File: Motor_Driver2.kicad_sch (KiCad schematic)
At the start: 20 parts, among them J701 Conn_01x02_Socket, U701 DMHT6016LFJ-13, U702 DRV8701

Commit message: all layouts re-designed.Next step routing...
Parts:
- C704: footprint Capacitor_SMD:C_Elec_8x10.2 -> Capacitor_SMD:CP_Elec_8x10; now left out of the parts list
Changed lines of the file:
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@@
 		(at 156.5298 86.0634 0)
 		(unit 1)
-		(exclude_from_sim no)
-		(in_bom yes)
-		(on_board yes)
+		(exclude_from_sim yes)
+		(in_bom no)
+		(on_board no)
 		(dnp no)
 		(property "Reference" "C704"
@@
 			)
 		)
-		(property "Footprint" "Capacitor_SMD:C_Elec_8x10.2"
+		(property "Footprint" "Capacitor_SMD:CP_Elec_8x10"
 			(at 156.5298 86.0634 0)
 			(effects

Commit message: ethernet, usb and motor driver-2 block routed, analog and digital planes seperated
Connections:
- net GND: now also U702.25 (GND)
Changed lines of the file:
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@@
 	(wire
 		(pts
+			(xy 132.4884 129.4869) (xy 135.7764 129.4869)
+		)
+		(stroke
+			(width 0)
+			(type default)
+		)
+	)
+	(wire
+		(pts
 			(xy 88.1048 90.2456) (xy 97.0671 90.2456)
 		)
@@
 	(wire
 		(pts
+			(xy 135.7764 129.4869) (xy 135.7764 139.1714)
+		)
+		(stroke
+			(width 0)
+			(type default)
+		)
+	)
+	(wire
+		(pts
 			(xy 119.8075 79.9351) (xy 119.8075 78.631)
 		)
@@
 	(wire
 		(pts
+			(xy 135.843 139.1714) (xy 135.7764 139.1714)
+		)
+		(stroke
+			(width 0)
+			(type default)
+		)
+	)
+	(wire
+		(pts
 			(xy 225.0723 120.7755) (xy 225.0723 121.7812)
 		)
@@
 		(pin "5"
 		)
+		(pin "25"
+		)
 		(instances
 			(project "mixed signal board project"
@@
 					(unit 1)
 				)
+			)
+		)
+	)
+	(symbol
+		(lib_id "power:GND")
+		(at 135.843 139.1714 0)
+		(unit 1)
+		(exclude_from_sim no)
+		(in_bom yes)
+		(on_board yes)
+		(dnp no)
+		(property "Reference" "#PWR0416"
+			(at 135.843 145.5214 0)
+			(effects
+				(font
+					(size 1.27 1.27)
+				)
+				(hide yes)
+			)
+		)
+		(property "Value" "GND"
+			(at 135.99 142.8958 0)
+			(effects
+				(font
+					(size 1.27 1.27)
+				)
+			)
+		)
+		(property "Footprint" ""
+			(at 135.843 139.1714 0)
+			(effects
+				(font
+					(size 1.27 1.27)
+				)
+				(hide yes)
+			)
+		)
+		(property "Datasheet" ""
+			(at 135.843 139.1714 0)
+			(effects
+				(font
+					(size 1.27 1.27)
+				)
+				(hide yes)
+			)
+		)
+		(property "Description" "Power symbol creates a global label with name \"GND\" , ground"
+			(at 135.843 139.1714 0)
+			(effects
+				(font
+					(size 1.27 1.27)
+				)
+				(hide yes)
+			)
+		)
+		(pin "1"
+		)
+		(instances
+			(project "mixed signal board project"
+				(path "/8a424437-6f3e-424c-a786-3b8b285eee60/fd70bbc0-4293-4cb1-946c-bcfbb1973be8"
+					(reference "#PWR0416")
+					(unit 1)
+				)

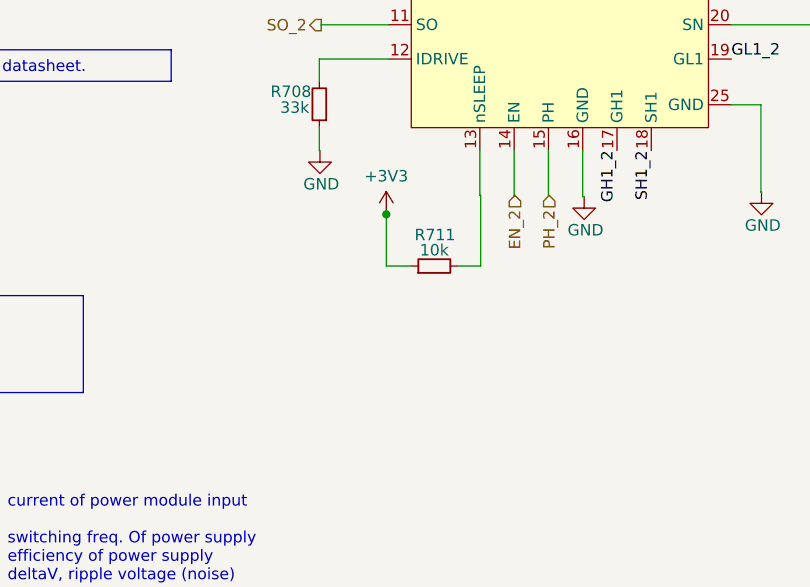
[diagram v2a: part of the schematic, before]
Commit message: motor driver nsleep pin pull-up resistor connected 12V plane by 3.3V voltage divider.
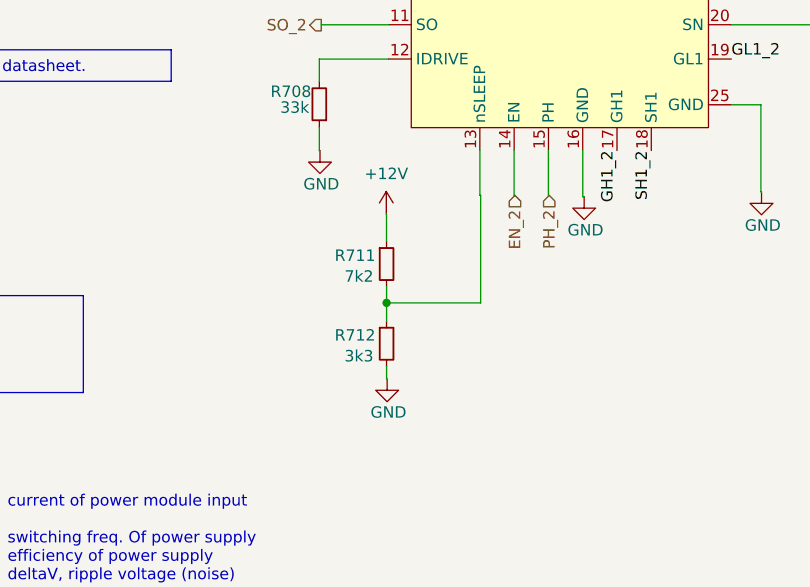
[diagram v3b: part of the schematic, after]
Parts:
- added R712: 3k3, Resistor_SMD:R_0805_2012Metric_Pad1.20x1.40mm_HandSolder, symbol Device:R_Small
- R711: value 10k -> 7k2
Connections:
- net +3V3 is gone; now on net +12V: R711.1
- net GND: now also R712.2
- net at R711.2, U702.13 (nSLEEP): now also R712.1
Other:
- moved on the sheet: R711
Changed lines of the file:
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@@
-	)
-	(junction
-		(at 94.1551 141.6614)
-		(diameter 0)
-		(color 0 0 0 0)
 	)
 	(junction
@@
 	)
 	(junction
+		(at 94.1837 151.4988)
+		(diameter 0)
+		(color 0 0 0 0)
+	)
+	(junction
 		(at 143.8069 81.3086)
 		(diameter 0)
@@
 	(wire
 		(pts
+			(xy 94.1757 141.6614) (xy 94.1757 144.6437)
+		)
+		(stroke
+			(width 0)
+			(type default)
+		)
+	)
+	(wire
+		(pts
 			(xy 59.9681 90.275) (xy 59.9681 92.1803)
 		)
@@
 	(wire
 		(pts
+			(xy 94.1837 158.58) (xy 94.1837 159.9414)
+		)
+		(stroke
+			(width 0)
+			(type default)
+		)
+	)
+	(wire
+		(pts
 			(xy 64.968 115.5816) (xy 64.968 116.7869)
 		)
@@
 	(wire
 		(pts
+			(xy 94.1837 159.9414) (xy 94.2463 159.9414)
+		)
+		(stroke
+			(width 0)
+			(type default)
+		)
+	)
+	(wire
+		(pts
 			(xy 168.1415 150.7108) (xy 168.0399 150.7108)
 		)
@@
 	(wire
 		(pts
-			(xy 94.1551 147.4049) (xy 94.1551 141.6614)
-		)
-		(stroke
-			(width 0)
-			(type default)
-		)
-	)
-	(wire
-		(pts
 			(xy 65.0488 109.1669) (xy 60.5986 109.1669)
 		)
@@
 	(wire
 		(pts
+			(xy 94.1757 144.6437) (xy 94.1837 144.6437)
+		)
+		(stroke
+			(width 0)
+			(type default)
+		)
+	)
+	(wire
+		(pts
+			(xy 94.1837 151.4988) (xy 94.1837 153.5)
+		)
+		(stroke
+			(width 0)
+			(type default)
+		)
+	)
+	(wire
+		(pts
 			(xy 159.0733 126.3206) (xy 163.1338 126.3206)
 		)
@@
 	(wire
 		(pts
-			(xy 102.0283 147.4049) (xy 104.6392 147.4049)
-		)
-		(stroke
-			(width 0)
-			(type default)
-		)
-	)
-	(wire
-		(pts
 			(xy 156.5298 90.2469) (xy 143.57 90.2469)
 		)
@@
 	(wire
 		(pts
+			(xy 104.6392 151.4988) (xy 94.1837 151.4988)
+		)
+		(stroke
+			(width 0)
+			(type default)
+		)
+	)
+	(wire
+		(pts
 			(xy 123.5984 91.8686) (xy 130.6565 91.8686)
 		)
@@
 	(wire
 		(pts
+			(xy 94.1837 149.7237) (xy 94.1837 151.4988)
+		)
+		(stroke
+			(width 0)
+			(type default)
+		)
+	)
+	(wire
+		(pts
 			(xy 79.5667 90.2852) (xy 70.2699 90.2852)
 		)
@@
 	(wire
 		(pts
+			(xy 104.6392 139.5566) (xy 104.6392 151.4988)
+		)
+		(stroke
+			(width 0)
+			(type default)
+		)
+	)
+	(wire
+		(pts
 			(xy 143.8069 81.3086) (xy 153.544 81.3086)
 		)
@@
 	(wire
 		(pts
-			(xy 96.9483 147.4049) (xy 94.1551 147.4049)
-		)
-		(stroke
-			(width 0)
-			(type default)
-		)
-	)
-	(wire
-		(pts
 			(xy 116.6311 78.6426) (xy 116.6837 88.2698)
 		)
@@
 		(pts
 			(xy 220.0448 116.7012) (xy 216.346 116.7012)
-		)
-		(stroke
-			(width 0)
-			(type default)
-		)
-	)
-	(wire
-		(pts
-			(xy 104.6392 147.4049) (xy 104.6392 139.5566)
 		)
 		(stroke
@@
 	(symbol
 		(lib_id "Device:R_Small")
-		(at 99.4883 147.4049 90)
+		(at 94.1837 147.1837 0)
 		(unit 1)
 		(exclude_from_sim no)
@@
 		(dnp no)
 		(property "Reference" "R711"
-			(at 99.5589 143.9472 90)
-			(effects
-				(font
-					(size 1.27 1.27)
-				)
-			)
-		)
-		(property "Value" "10k"
-			(at 99.4883 145.6408 90)
+			(at 90.6816 146.2457 0)
+			(effects
+				(font
+					(size 1.27 1.27)
+				)
+			)
+		)
+		(property "Value" "7k2"
+			(at 91.1194 148.5596 0)
 			(effects
 				(font
@@
 		)
 		(property "Footprint" "Resistor_SMD:R_0805_2012Metric_Pad1.20x1.40mm_HandSolder"
-			(at 99.4883 147.4049 0)
+			(at 94.1837 147.1837 0)
 			(effects
 				(font
@@
 		)
 		(property "Datasheet" "~"
-			(at 99.4883 147.4049 0)
+			(at 94.1837 147.1837 0)
 			(effects
 				(font
@@
 		)
 		(property "Description" "Resistor, small symbol"
-			(at 99.4883 147.4049 0)
+			(at 94.1837 147.1837 0)
 			(effects
 				(font
@@
 				(path "/8a424437-6f3e-424c-a786-3b8b285eee60/fd70bbc0-4293-4cb1-946c-bcfbb1973be8"
 					(reference "R701")
+					(unit 1)
+				)
+			)
+		)
+	)
+	(symbol
+		(lib_id "power:GND")
+		(at 94.2463 159.9414 0)
+		(unit 1)
+		(exclude_from_sim no)
+		(in_bom yes)
+		(on_board yes)
+		(dnp no)
+		(property "Reference" "#PWR0809"
+			(at 94.2463 166.2914 0)
+			(effects
+				(font
+					(size 1.27 1.27)
+				)
+				(hide yes)
+			)
+		)
+		(property "Value" "GND"
+			(at 94.3933 163.6658 0)
+			(effects
+				(font
+					(size 1.27 1.27)
+				)
+			)
+		)
+		(property "Footprint" ""
+			(at 94.2463 159.9414 0)
+			(effects
+				(font
+					(size 1.27 1.27)
+				)
+				(hide yes)
+			)
+		)
+		(property "Datasheet" ""
+			(at 94.2463 159.9414 0)
+			(effects
+				(font
+					(size 1.27 1.27)
+				)
+				(hide yes)
+			)
+		)
+		(property "Description" "Power symbol creates a global label with name \"GND\" , ground"
+			(at 94.2463 159.9414 0)
+			(effects
+				(font
+					(size 1.27 1.27)
+				)
+				(hide yes)
+			)
+		)
+		(pin "1"
+		)
+		(instances
+			(project "mixed signal board project"
+				(path "/8a424437-6f3e-424c-a786-3b8b285eee60/fd70bbc0-4293-4cb1-946c-bcfbb1973be8"
+					(reference "#PWR0809")
 					(unit 1)
 				)
@@
 	)
 	(symbol
+		(lib_id "Device:R_Small")
+		(at 94.1837 156.04 0)
+		(unit 1)
+		(exclude_from_sim no)
+		(in_bom yes)
+		(on_board yes)
+		(dnp no)
+		(property "Reference" "R712"
+			(at 90.6816 155.102 0)
+			(effects
+				(font
+					(size 1.27 1.27)
+				)
+			)
+		)
+		(property "Value" "3k3"
+			(at 91.1194 157.4159 0)
+			(effects
+				(font
+					(size 1.27 1.27)
+				)
+			)
+		)
+		(property "Footprint" "Resistor_SMD:R_0805_2012Metric_Pad1.20x1.40mm_HandSolder"
+			(at 94.1837 156.04 0)
+			(effects
+				(font
+					(size 1.27 1.27)
+				)
+				(hide yes)
+			)
+		)
+		(property "Datasheet" "~"
+			(at 94.1837 156.04 0)
+			(effects
+				(font
+					(size 1.27 1.27)
+				)
+				(hide yes)
+			)
+		)
+		(property "Description" "Resistor, small symbol"
+			(at 94.1837 156.04 0)
+			(effects
+				(font
+					(size 1.27 1.27)
+				)
+				(hide yes)
+			)
+		)
+		(pin "1"
+		)
+		(pin "2"
+		)
+		(instances
+			(project "mixed signal board project"
+				(path "/8a424437-6f3e-424c-a786-3b8b285eee60/fd70bbc0-4293-4cb1-946c-bcfbb1973be8"
+					(reference "R712")
+					(unit 1)
+				)
+			)
+		)
+	)
+	(symbol
 		(lib_id "power:GND")
 		(at 168.0399 150.7108 0)
@@
 			)
 		)
-		(property "Value" "+3V3"
-			(at 94.1551 137.42 0)
-			(effects
-				(font
+		(property "Value" "+12V"
+			(at 94.1551 137.16 0)
+			(effects
+				(font

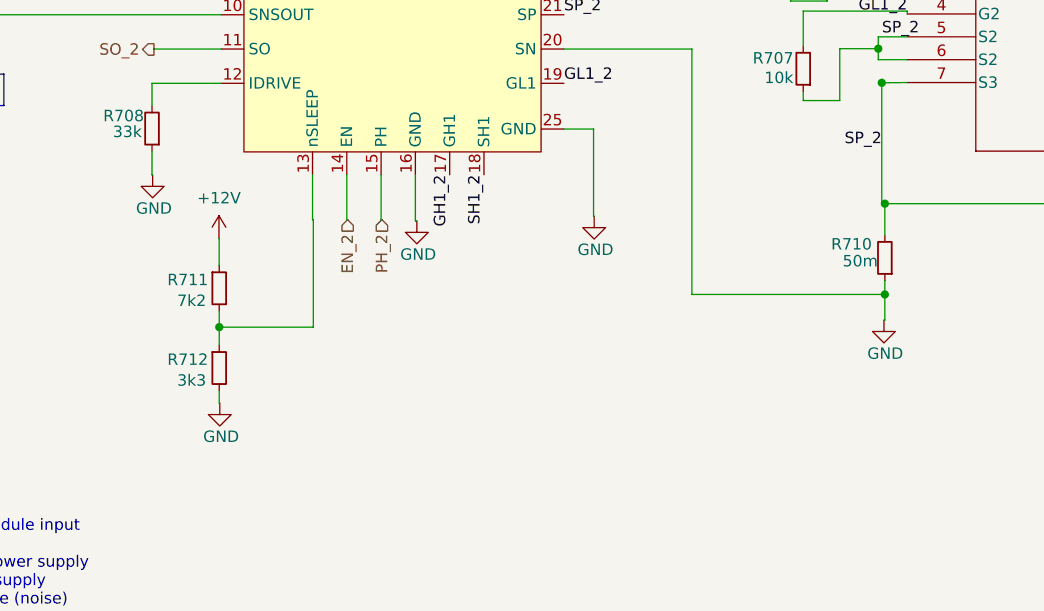
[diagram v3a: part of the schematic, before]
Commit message: some design failures reviewed(MIC VDD is 1V8, Motor Drivers' pull-up to DVDD pin, I2C net fixed). Routing mostly done.
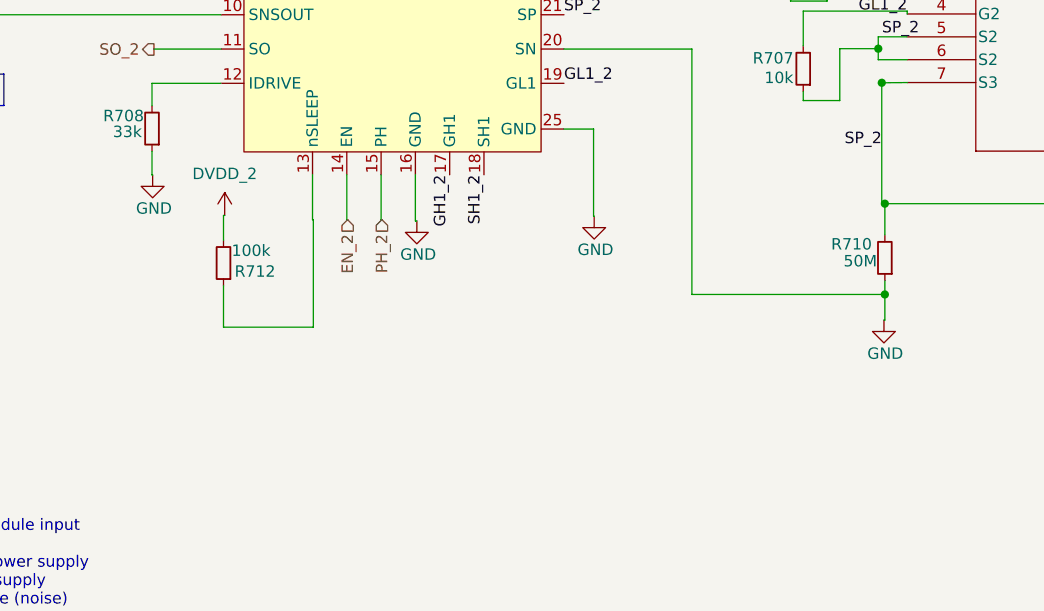
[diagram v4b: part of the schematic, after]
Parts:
- removed R711: 7k2, Resistor_SMD:R_0805_2012Metric_Pad1.20x1.40mm_HandSolder, symbol Device:R_Small
- R710: value 50m -> 50M
- R712: value 3k3 -> 100k
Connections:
- net DVDD_2: now also R712.2
- net GND: no longer R712.2
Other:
- moved on the sheet: R712
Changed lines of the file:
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@@
 	)
 	(junction
-		(at 94.1837 151.4988)
-		(diameter 0)
-		(color 0 0 0 0)
-	)
-	(junction
 		(at 143.8069 81.3086)
 		(diameter 0)
@@
 	(wire
 		(pts
-			(xy 119.7884 79.9351) (xy 119.7884 96.4669)
+			(xy 94.6584 141.8331) (xy 94.6584 139.0842)
 		)
 		(stroke
@@
 	(wire
 		(pts
-			(xy 104.5484 134.5669) (xy 104.5484 139.5566)
+			(xy 119.7884 79.9351) (xy 119.7884 96.4669)
 		)
 		(stroke
@@
 	(wire
 		(pts
-			(xy 89.1599 111.4154) (xy 89.1599 112.9769)
+			(xy 104.5484 134.5669) (xy 104.5484 139.5566)
 		)
 		(stroke
@@
 	(wire
 		(pts
-			(xy 73.6581 104.3984) (xy 73.6581 109.1669)
+			(xy 89.1599 111.4154) (xy 89.1599 112.9769)
 		)
 		(stroke
@@
 	(wire
 		(pts
-			(xy 79.4571 111.4154) (xy 79.4571 109.1669)
+			(xy 73.6581 104.3984) (xy 73.6581 109.1669)
 		)
 		(stroke
@@
 	(wire
 		(pts
-			(xy 94.1757 141.6614) (xy 94.1757 144.6437)
+			(xy 79.4571 111.4154) (xy 79.4571 109.1669)
 		)
 		(stroke
@@
 	(wire
 		(pts
-			(xy 94.1837 158.58) (xy 94.1837 159.9414)
-		)
-		(stroke
-			(width 0)
-			(type default)
-		)
-	)
-	(wire
-		(pts
 			(xy 64.968 115.5816) (xy 64.968 116.7869)
 		)
@@
 	(wire
 		(pts
-			(xy 94.1837 159.9414) (xy 94.2463 159.9414)
-		)
-		(stroke
-			(width 0)
-			(type default)
-		)
-	)
-	(wire
-		(pts
 			(xy 168.1415 150.7108) (xy 168.0399 150.7108)
 		)
@@
 	(wire
 		(pts
-			(xy 97.0671 96.4669) (xy 97.0671 90.2456)
+			(xy 94.6584 139.0842) (xy 94.794 139.0842)
 		)
 		(stroke
@@
 	(wire
 		(pts
-			(xy 94.1551 141.6614) (xy 94.1757 141.6614)
+			(xy 97.0671 96.4669) (xy 97.0671 90.2456)
 		)
 		(stroke
@@
 	(wire
 		(pts
-			(xy 94.1757 144.6437) (xy 94.1837 144.6437)
-		)
-		(stroke
-			(width 0)
-			(type default)
-		)
-	)
-	(wire
-		(pts
-			(xy 94.1837 151.4988) (xy 94.1837 153.5)
+			(xy 94.6584 151.4988) (xy 94.6584 146.9131)
 		)
 		(stroke
@@
 	(wire
 		(pts
-			(xy 104.6392 151.4988) (xy 94.1837 151.4988)
+			(xy 104.6392 151.4988) (xy 94.6584 151.4988)
 		)
 		(stroke
@@
 	(wire
 		(pts
-			(xy 94.1837 149.7237) (xy 94.1837 151.4988)
-		)
-		(stroke
-			(width 0)
-			(type default)
-		)
-	)
-	(wire
-		(pts
 			(xy 79.5667 90.2852) (xy 70.2699 90.2852)
 		)
@@
 	(symbol
 		(lib_id "Device:R_Small")
-		(at 94.1837 147.1837 0)
-		(unit 1)
-		(exclude_from_sim no)
-		(in_bom yes)
-		(on_board yes)
-		(dnp no)
-		(property "Reference" "R711"
-			(at 90.6816 146.2457 0)
-			(effects
-				(font
-					(size 1.27 1.27)
-				)
-			)
-		)
-		(property "Value" "7k2"
-			(at 91.1194 148.5596 0)
-			(effects
-				(font
-					(size 1.27 1.27)
-				)
-			)
-		)
-		(property "Footprint" "Resistor_SMD:R_0805_2012Metric_Pad1.20x1.40mm_HandSolder"
-			(at 94.1837 147.1837 0)
-			(effects
-				(font
-					(size 1.27 1.27)
-				)
-				(hide yes)
-			)
-		)
-		(property "Datasheet" "~"
-			(at 94.1837 147.1837 0)
-			(effects
-				(font
-					(size 1.27 1.27)
-				)
-				(hide yes)
-			)
-		)
-		(property "Description" "Resistor, small symbol"
-			(at 94.1837 147.1837 0)
-			(effects
-				(font
-					(size 1.27 1.27)
-				)
-				(hide yes)
-			)
-		)
-		(pin "1"
-		)
-		(pin "2"
-		)
-		(instances
-			(project "mixed signal board project"
-				(path "/8a424437-6f3e-424c-a786-3b8b285eee60/fd70bbc0-4293-4cb1-946c-bcfbb1973be8"
-					(reference "R711")
-					(unit 1)
-				)
-			)
-		)
-	)
-	(symbol
-		(lib_id "Device:R_Small")
 		(at 100.8776 90.175 90)
 		(unit 1)
@@
 	)
 	(symbol
-		(lib_id "power:GND")
-		(at 94.2463 159.9414 0)
+		(lib_id "power:PWR_FLAG")
+		(at 73.6581 104.3984 0)
 		(unit 1)
 		(exclude_from_sim no)
@@
 		(on_board yes)
 		(dnp no)
-		(property "Reference" "#PWR0809"
-			(at 94.2463 166.2914 0)
+		(fields_autoplaced yes)
+		(property "Reference" "#FLG0403"
+			(at 73.6581 102.4934 0)
 			(effects
 				(font
@@
 			)
 		)
-		(property "Value" "GND"
-			(at 94.3933 163.6658 0)
+		(property "Value" "PWR_FLAG"
+			(at 73.6581 98.9773 0)
 			(effects
 				(font
@@
 		)
 		(property "Footprint" ""
-			(at 94.2463 159.9414 0)
+			(at 73.6581 104.3984 0)
 			(effects
 				(font
@@
 			)
 		)
-		(property "Datasheet" ""
-			(at 94.2463 159.9414 0)
+		(property "Datasheet" "~"
+			(at 73.6581 104.3984 0)
 			(effects
 				(font
@@
 			)
 		)
-		(property "Description" "Power symbol creates a global label with name \"GND\" , ground"
-			(at 94.2463 159.9414 0)
+		(property "Description" "Special symbol for telling ERC where power comes from"
+			(at 73.6581 104.3984 0)
 			(effects
 				(font
@@
 			(project "mixed signal board project"
 				(path "/8a424437-6f3e-424c-a786-3b8b285eee60/fd70bbc0-4293-4cb1-946c-bcfbb1973be8"
-					(reference "#PWR0809")
+					(reference "#FLG0403")
 					(unit 1)
 				)
@@
 	)
 	(symbol
-		(lib_id "power:PWR_FLAG")
-		(at 73.6581 104.3984 0)
+		(lib_id "power:VDD")
+		(at 94.794 139.0842 0)
 		(unit 1)
 		(exclude_from_sim no)
@@
 		(dnp no)
 		(fields_autoplaced yes)
-		(property "Reference" "#FLG0403"
-			(at 73.6581 102.4934 0)
+		(property "Reference" "#PWR0506"
+			(at 94.794 142.8942 0)
 			(effects
 				(font
@@
 			)
 		)
-		(property "Value" "PWR_FLAG"
-			(at 73.6581 98.9773 0)
+		(property "Value" "DVDD_2"
+			(at 94.794 134.4623 0)
 			(effects
 				(font
@@
 		)
 		(property "Footprint" ""
-			(at 73.6581 104.3984 0)
+			(at 94.794 139.0842 0)
 			(effects
 				(font
@@
 			)
 		)
-		(property "Datasheet" "~"
-			(at 73.6581 104.3984 0)
+		(property "Datasheet" ""
+			(at 94.794 139.0842 0)
 			(effects
 				(font
@@
 			)
 		)
-		(property "Description" "Special symbol for telling ERC where power comes from"
-			(at 73.6581 104.3984 0)
+		(property "Description" "Power symbol creates a global label with name \"VDD\""
+			(at 94.794 139.0842 0)
 			(effects
 				(font
@@
 			(project "mixed signal board project"
 				(path "/8a424437-6f3e-424c-a786-3b8b285eee60/fd70bbc0-4293-4cb1-946c-bcfbb1973be8"
-					(reference "#FLG0403")
+					(reference "#PWR0506")
 					(unit 1)
 				)
@@
 			)
 		)
-		(property "Value" "50m"
+		(property "Value" "50M"
 			(at 165.407 144.1604 0)
 			(effects
@@
 	(symbol
 		(lib_id "Device:R_Small")
-		(at 94.1837 156.04 0)
+		(at 94.6584 144.3731 180)
 		(unit 1)
 		(exclude_from_sim no)
@@
 		(dnp no)
 		(property "Reference" "R712"
-			(at 90.6816 155.102 0)
+			(at 98.1605 145.3111 0)
 			(effects
 				(font
@@
 			)
 		)
-		(property "Value" "3k3"
-			(at 91.1194 157.4159 0)
+		(property "Value" "100k"
+			(at 97.7227 142.9972 0)
 			(effects
 				(font
@@
 		)
 		(property "Footprint" "Resistor_SMD:R_0805_2012Metric_Pad1.20x1.40mm_HandSolder"
-			(at 94.1837 156.04 0)
+			(at 94.6584 144.3731 0)
 			(effects
 				(font
@@
 		)
 		(property "Datasheet" "~"
-			(at 94.1837 156.04 0)
+			(at 94.6584 144.3731 0)
 			(effects
 				(font
@@
 		)
 		(property "Description" "Resistor, small symbol"
-			(at 94.1837 156.04 0)
+			(at 94.6584 144.3731 0)
 			(effects
 				(font
@@
 					(unit 1)
 				)
-			)
-		)
-	)
-	(symbol
-		(lib_id "power:+3V3")
-		(at 94.1551 141.6614 0)
-		(unit 1)
-		(exclude_from_sim no)
-		(in_bom yes)
-		(on_board yes)
-		(dnp no)
-		(fields_autoplaced yes)
-		(property "Reference" "#PWR0406"
-			(at 94.1551 145.4714 0)
-			(effects
-				(font
-					(size 1.27 1.27)
-				)
-				(hide yes)
-			)
-		)
-		(property "Value" "+12V"
-			(at 94.1551 137.16 0)
-			(effects
-				(font
-					(size 1.27 1.27)
-				)
-			)
-		)
-		(property "Footprint" ""
-			(at 94.1551 141.6614 0)
-			(effects
-				(font
-					(size 1.27 1.27)
-				)
-				(hide yes)
-			)
-		)
-		(property "Datasheet" ""
-			(at 94.1551 141.6614 0)
-			(effects
-				(font
-					(size 1.27 1.27)
-				)
-				(hide yes)
-			)
-		)
-		(property "Description" "Power symbol creates a global label with name \"+3V3\""
-			(at 94.1551 141.6614 0)
-			(effects
-				(font
-					(size 1.27 1.27)
-				)
-				(hide yes)
-			)
-		)
-		(pin "1"
-		)
-		(instances
-			(project ""
-				(path "/8a424437-6f3e-424c-a786-3b8b285eee60/fd70bbc0-4293-4cb1-946c-bcfbb1973be8"
-					(reference "#PWR0406")
-					(unit 1)
-				)

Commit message: some additions
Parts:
- renumbered C704 to C?, C702 to C?, C706 to C?, C705 to C?, C703 to C?, C701 to C?, J701 to J?, R701 to R?, R706 to R?, R710 to R?, R709 to R?, R705 to R?, R702 to R?, R712 to R?, R708 to R?, R703 to R?, R707 to R?, R704 to R?, U701 to U?, U702 to U?
